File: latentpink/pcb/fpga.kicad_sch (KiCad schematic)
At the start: 39 parts, among them J9 XILINX_JTAG, M2 960-23-23-F-AB-0, U2 XC7K160T-2FBG484C

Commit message: Finished initial schematic, ready for design review
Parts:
- C156, C160, C161: footprint (none) -> azonenberg_pcb:EIA_1206_CAP_NOSILK
- FB2, FB3, FB4: value TBD -> BLM31KN271SH1L; footprint (none) -> azonenberg_pcb:EIA_1206_CAP_NOSILK
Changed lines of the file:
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@@
     (in_bom yes) (on_board yes) (fields_autoplaced)
     (property "Reference" "FB3" (id 0) (at 162.56 190.1022 0))
-    (property "Value" "TBD" (id 1) (at 162.56 192.6391 0))
-    (property "Footprint" "" (id 2) (at 162.56 194.31 0)
+    (property "Value" "BLM31KN271SH1L" (id 1) (at 162.56 192.6391 0))
+    (property "Footprint" "azonenberg_pcb:EIA_1206_CAP_NOSILK" (id 2) (at 162.56 194.31 0)
       (effects (font (size 1.524 1.524)) hide)
     )
@@
     (in_bom yes) (on_board yes) (fields_autoplaced)
     (property "Reference" "FB2" (id 0) (at 162.56 176.1322 0))
-    (property "Value" "TBD" (id 1) (at 162.56 178.6691 0))
-    (property "Footprint" "" (id 2) (at 162.56 180.34 0)
+    (property "Value" "BLM31KN271SH1L" (id 1) (at 162.56 178.6691 0))
+    (property "Footprint" "azonenberg_pcb:EIA_1206_CAP_NOSILK" (id 2) (at 162.56 180.34 0)
       (effects (font (size 1.524 1.524)) hide)
     )
@@
       (effects (font (size 1.27 1.27)) (justify left))
     )
-    (property "Footprint" "" (id 2) (at 41.6052 217.17 0)
+    (property "Footprint" "azonenberg_pcb:EIA_1206_CAP_NOSILK" (id 2) (at 41.6052 217.17 0)
       (effects (font (size 1.27 1.27)) hide)
     )
@@
     (in_bom yes) (on_board yes) (fields_autoplaced)
     (property "Reference" "FB4" (id 0) (at 162.56 204.0722 0))
-    (property "Value" "TBD" (id 1) (at 162.56 206.6091 0))
-    (property "Footprint" "" (id 2) (at 162.56 208.28 0)
+    (property "Value" "BLM31KN271SH1L" (id 1) (at 162.56 206.6091 0))
+    (property "Footprint" "azonenberg_pcb:EIA_1206_CAP_NOSILK" (id 2) (at 162.56 208.28 0)
       (effects (font (size 1.524 1.524)) hide)
     )
@@
     (pin "2")
   )
-  (symbol (lib_id "xilinx-azonenberg:XC7KxT-FBG484") (at 176.53 151.13 0) (unit 2)
+  (symbol (lib_name "XC7KxT-FBG484_2") (lib_id "xilinx-azonenberg:XC7KxT-FBG484") (at 176.53 151.13 0) (unit 2)
     (in_bom yes) (on_board yes)
     (property "Reference" "U2" (id 0) (at 187.96 153.67 0)
@@
       (effects (font (size 1.27 1.27)) (justify left))
     )
-    (property "Footprint" "" (id 2) (at 54.3052 217.17 0)
+    (property "Footprint" "azonenberg_pcb:EIA_1206_CAP_NOSILK" (id 2) (at 54.3052 217.17 0)
       (effects (font (size 1.27 1.27)) hide)
     )
@@
     (pin "2")
   )
-  (symbol (lib_id "xilinx-azonenberg:XC7KxT-FBG484") (at 264.16 151.13 0) (unit 10)
+  (symbol (lib_name "XC7KxT-FBG484_1") (lib_id "xilinx-azonenberg:XC7KxT-FBG484") (at 264.16 151.13 0) (unit 10)
     (in_bom yes) (on_board yes)
     (property "Reference" "U2" (id 0) (at 274.32 154.94 0)
@@
       (effects (font (size 1.27 1.27)) (justify left))
     )
-    (property "Footprint" "" (id 2) (at 68.2752 187.96 0)
-      (effects (font (size 1.27 1.27)) hide)
-    )
+    (property "Footprint" "azonenberg_pcb:EIA_1206_CAP_NOSILK" (id 2) (at 68.2752 187.96 0)
+      (effects (font (size 1.27 1.27)) hide)
+    )

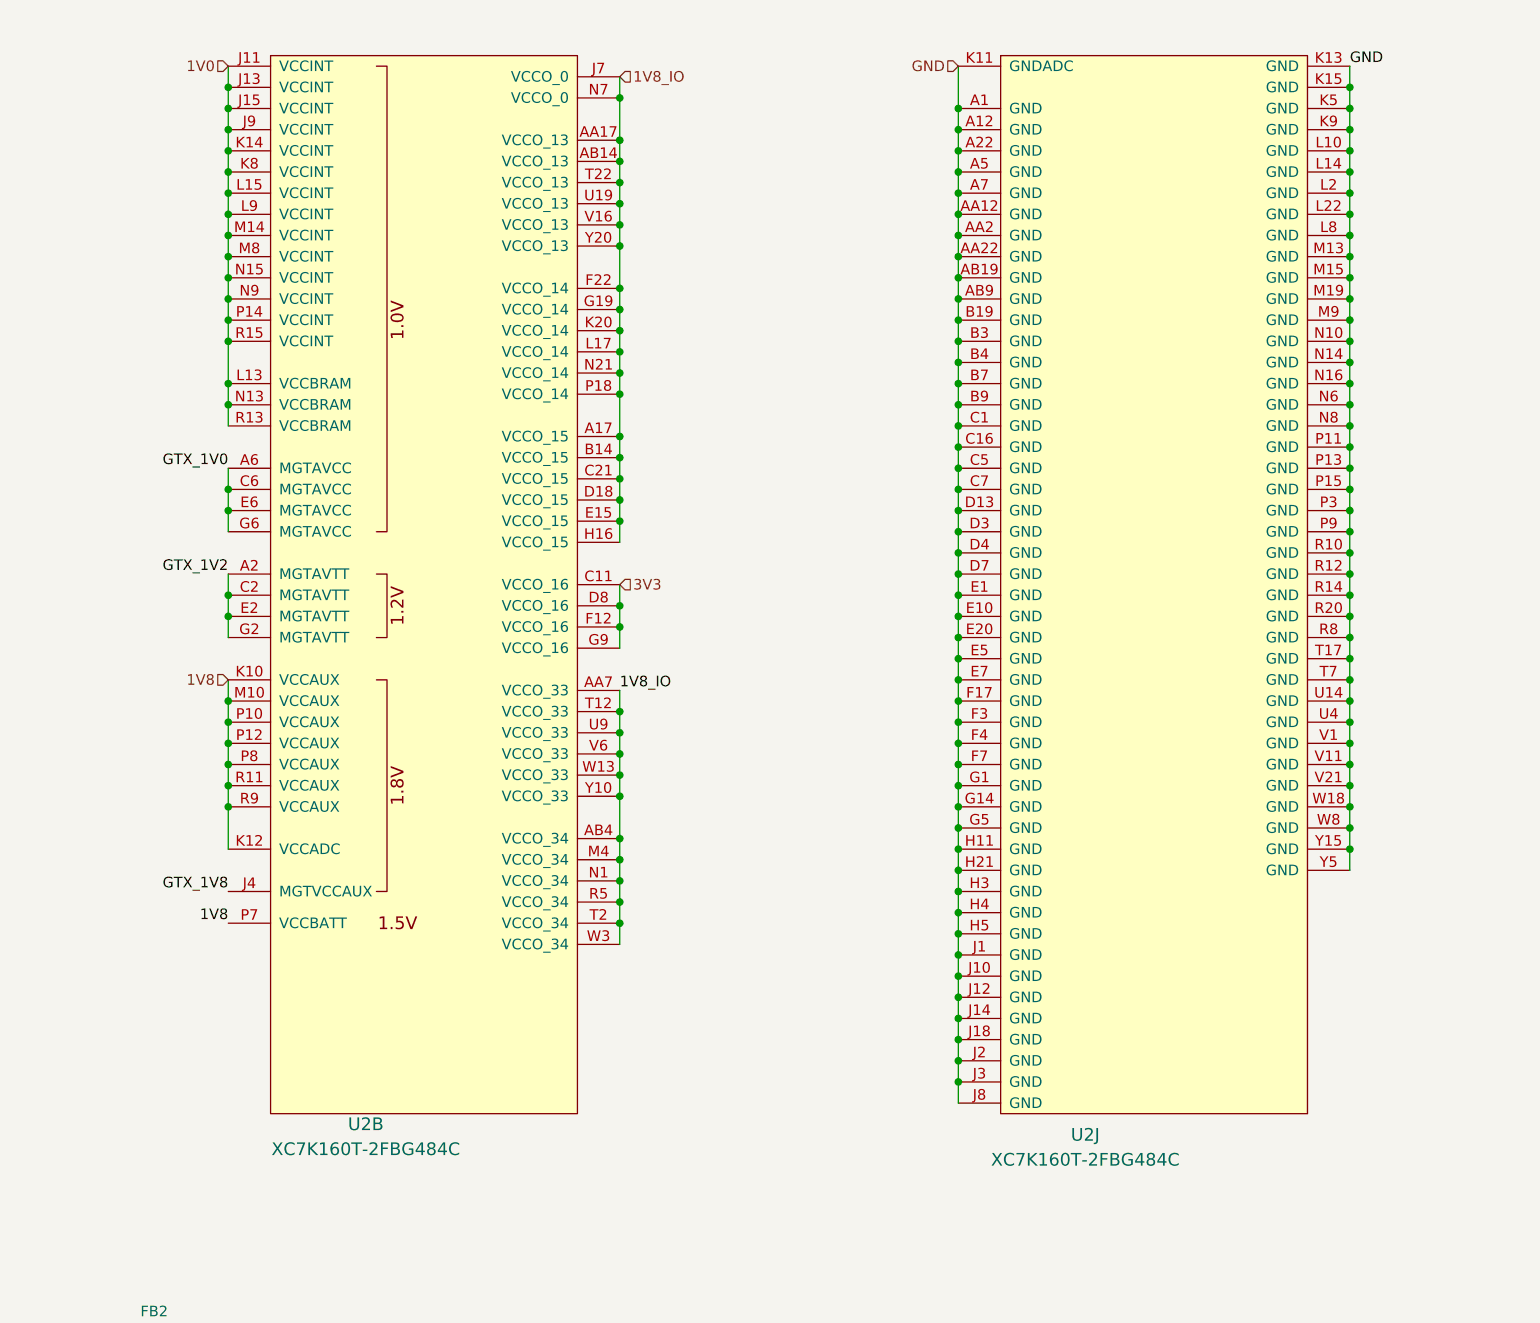
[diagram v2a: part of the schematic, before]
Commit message: Finished initial schematic review, added ESD diodes to Ethernet pairs
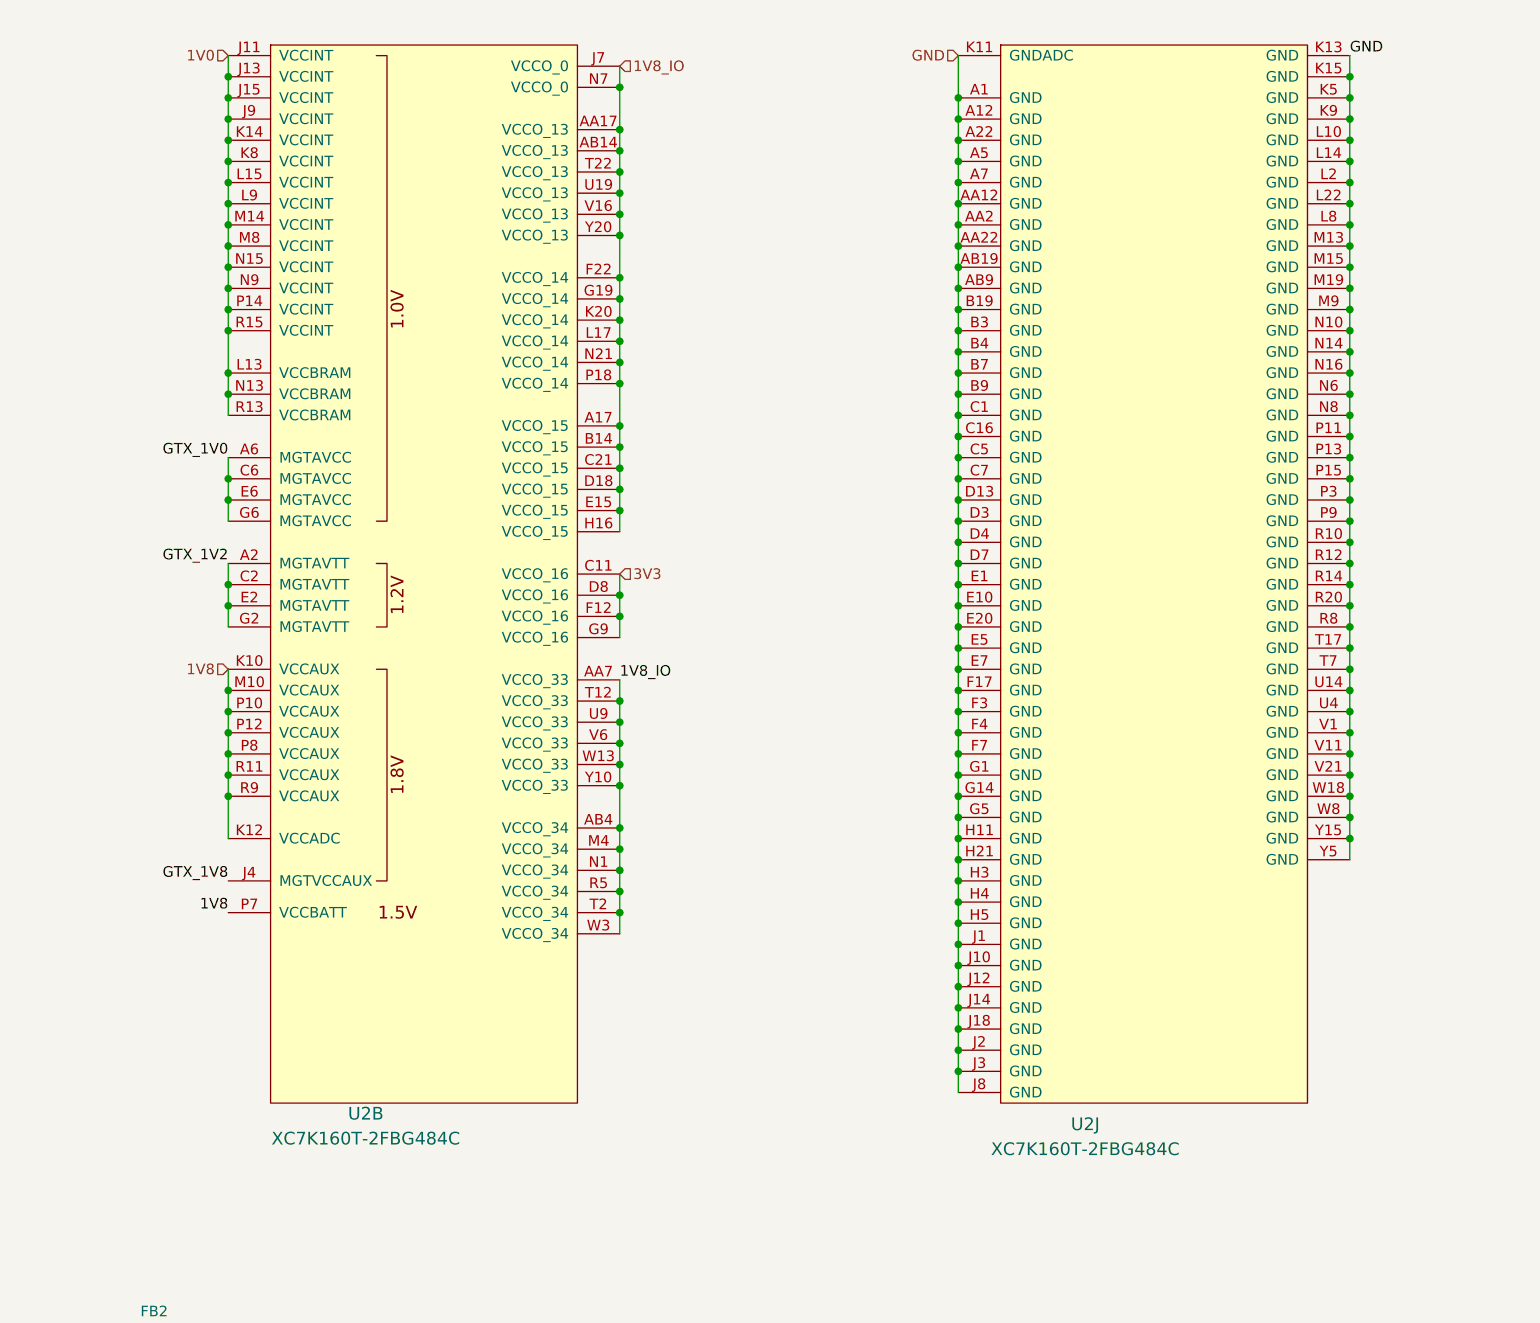
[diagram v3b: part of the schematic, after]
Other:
- moved on the sheet: U2B, U2J

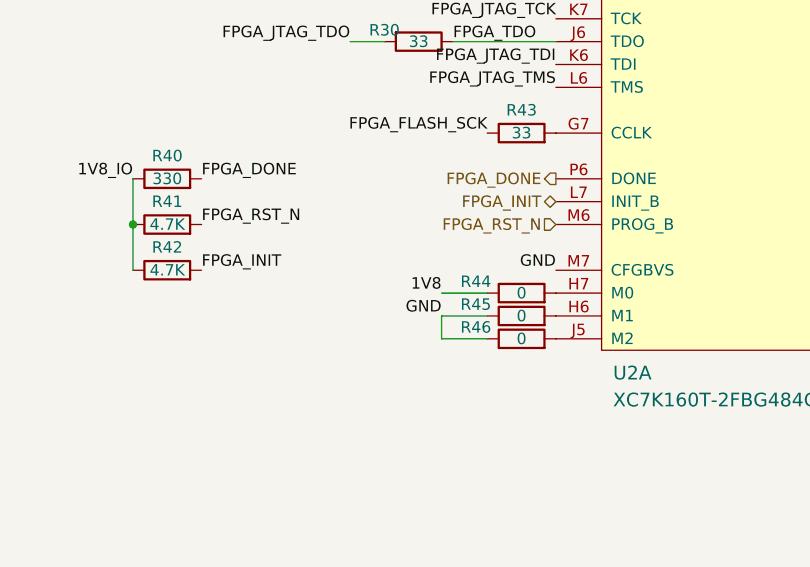
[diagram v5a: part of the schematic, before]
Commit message: Rearranged all unplaced components and grouped by functional subsystem
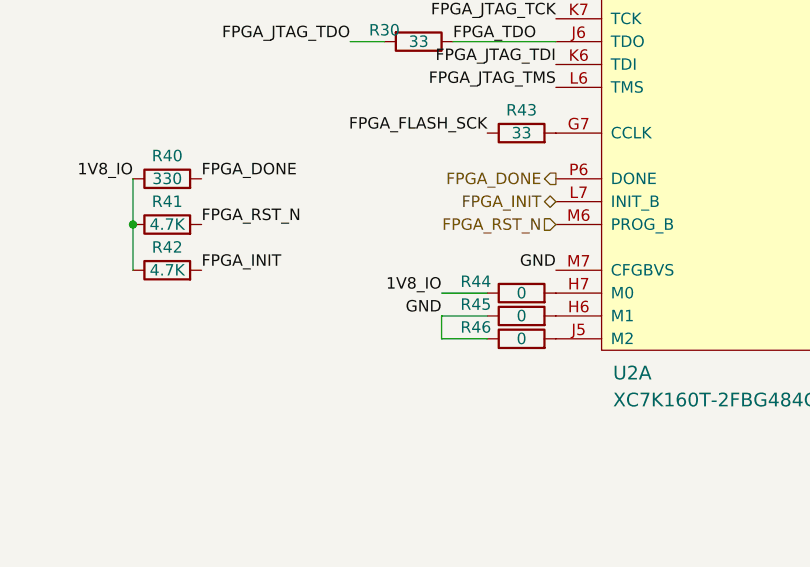
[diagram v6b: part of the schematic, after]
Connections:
- net 1V8: no longer R44.1
- net 1V8_IO: now also R44.1
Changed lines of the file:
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@@
     (effects (font (size 1.27 1.27)) (justify right bottom))
   )
-  (label "1V8" (at 83.82 144.78 180)
+  (label "1V8_IO" (at 83.82 144.78 180)
     (effects (font (size 1.27 1.27)) (justify right bottom))
   )

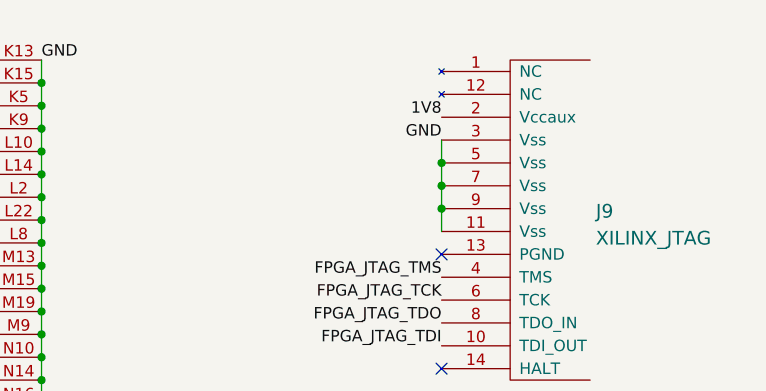
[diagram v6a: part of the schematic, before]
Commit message: Routed upper SGMII PHY except for bus to FPGA
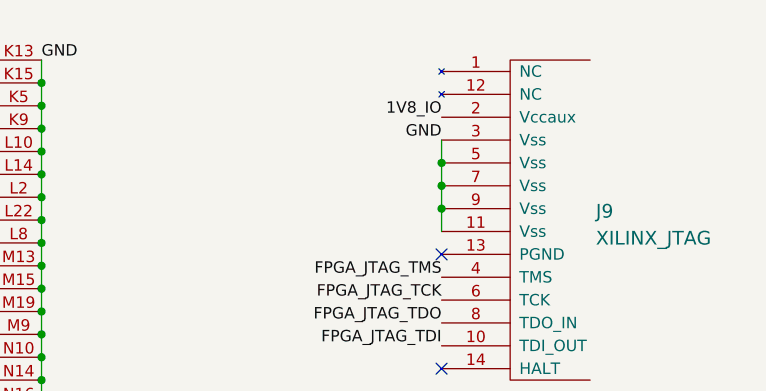
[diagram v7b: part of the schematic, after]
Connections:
- net 1V8: no longer J9.2 (Vccaux)
- net 1V8_IO: now also J9.2 (Vccaux)
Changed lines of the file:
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@@
   (paper "A3")
   (title_block
-    (date "2023-05-27")
+    (date "2023-05-28")
     (rev "0.1")
     (company "Antikernel Labs")
@@
     (effects (font (size 1.27 1.27)) (justify left bottom))
   )
-  (label "1V8" (at 350.52 31.75 180)
-    (effects (font (size 1.27 1.27)) (justify right bottom))
-  )
+  (label "1V8_IO" (at 350.52 31.75 180)
+    (effects (font (size 1.27 1.27)) (justify right bottom))
+  )
